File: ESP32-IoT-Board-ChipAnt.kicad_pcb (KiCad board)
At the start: 2 copper layers, 49 parts, among them IC1 ESP32-C3FH4, IC2 CP2102N-A02-GQFN28, J1 USB_B_Micro, Q1 Q_NPN_BEC, Q2 Q_NPN_BEC, U1 AMS1117-3.3, U2 USBLC6-2SC6, U3 MCP9700AT-ETT, Y1 40 Mhz Crystal

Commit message: First draft of PCB
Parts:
- removed C18: 10uF, Capacitor_SMD:C_0603_1608Metric
- removed the C3 at (160.9, 81.5)
- removed H4: MountingHole 3mm, MountingHole:MountingHole_3mm_Pad_Via
- removed MK1: INMP441ACEZ, INMP441:INMP441ACEZ
- removed R10: 10k, Resistor_SMD:R_0402_1005Metric
- removed the R3 at (144.8, 101.6)
- added C17: 10uF, Capacitor_SMD:C_0603_1608Metric, F.Cu at (150.4, 101.4)
- added J2: Conn_01x05, Connector_Molex:Molex_KK-254_AE-6410-05A_1x05_P2.54mm_Vertical, F.Cu at (138.4, 122.5)
- added R9: 10k, Resistor_SMD:R_0402_1005Metric, F.Cu at (150.1, 99.9)
- C12: renamed from C13; footprint Capacitor_SMD:C_0603_1608Metric -> Capacitor_SMD:C_0402_1005Metric
- C13: renamed from C14; footprint Capacitor_SMD:C_0603_1608Metric -> Capacitor_SMD:C_0402_1005Metric
- L2: footprint Inductor_SMD:L_0603_1608Metric -> Inductor_SMD:L_0402_1005Metric
- moved H1 73.2 mm to (123.0, 122.6)
- moved H2 56.8 mm to (123.0, 84.0)
- moved ANT1 46.7 mm to (162.8, 117.4), turned to 90 degrees
- moved Y1 41.4 mm to (145.9, 123.7), turned to 90 degrees
- moved C8 41.2 mm to (143.0, 123.8), turned to -90 degrees
- moved C13 36.4 mm to (152.1, 119.3), turned to -90 degrees
- moved C6 35.8 mm to (151.2, 124.6)
- moved C14 33.5 mm to (140.3, 115.3), turned to 180 degrees
- moved IC1 33.3 mm to (145.8, 117.1), turned to 180 degrees
- moved R6 31.6 mm to (151.8, 109.6)
- moved C5 30.2 mm to (151.2, 123.0)
- moved R1 27.3 mm to (128.6, 99.8)
- moved R4 26.8 mm to (140.3, 93.0)
- moved S1 26.2 mm to (146.0, 103.7), turned to 90 degrees
- moved L1 25.0 mm to (152.4, 115.6), turned to 180 degrees
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- renumbered C11 to C10, C12 to C11, C15 to C14, C16 to C15, C17 to C16, C4 to C3, C5 to C4, C6 to C5, C7 to C6, C8 to C7, C9 to C8, C10 to C9, R4 to R3, R5 to R4, R6 to R5, R7 to R6, R8 to R7, R9 to R8
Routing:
- net GND: track 0.00 -> 65.2 mm, vias 0 -> 59
- net +3V3: track 0.00 -> 63.7 mm, vias 0 -> 29
- net RXD0: track 0.00 -> 36.9 mm
- net TXD0: track 0.00 -> 36.5 mm
- net CHIP_EN: track 0.00 -> 30.0 mm, vias 0 -> 2
- net GPIO9: track 0.00 -> 26.9 mm, vias 0 -> 2
- net ADC_IN: track 0.00 -> 25.1 mm
- net VBUS: track 0.00 -> 19.3 mm, vias 0 -> 2
- net RTS: track 0.00 -> 14.4 mm, vias 0 -> 2
- net DTR: track 0.00 -> 14.2 mm, vias 0 -> 2
- net I2S_WS: track 0.00 -> 12.8 mm, vias 0 -> 2
- net unconnected-(J1-Pad6): track 0.00 -> 12.6 mm
- net D-: track 0.00 -> 11.9 mm
- net D+: track 0.00 -> 10.4 mm
- net I2S_SCK: track 0.00 -> 9.17 mm, vias 0 -> 2
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- added copper zone on B.Cu, net (none)
- added copper zone on F.Cu, net (none)
- added copper zone on In2.Cu, net +3V3
- added copper zone on In1.Cu, net GND
- added copper zone on F.Cu, net Net-(ANT1-Pad1)
- added copper zone on F.Cu, net unconnected-(ANT1-Pad2)
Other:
- board outline added: 45.6 x 45.6 mm
- copper layers 2 -> 4

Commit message: --
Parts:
- removed the C15 at (138.1, 108.8)
- removed IC2: CP2102N-A02-GQFN28, CP2102N-A02-GQFN28:QFN50P500X500X80-29N-D
- removed Q1, Q2: Q_NPN_BEC, Package_TO_SOT_SMD:SOT-23
- removed the R3 at (142.1, 96.4)
- removed the R4 at (140.3, 93.0)
- removed R7: 10k(NC), Resistor_SMD:R_0402_1005Metric
- removed R8: 1k, Resistor_SMD:R_0402_1005Metric
- added J3: Conn_01x05, Connector_PinHeader_2.54mm:PinHeader_1x05_P2.54mm_Vertical, F.Cu at (148.5, 96.0)
- added R5: 1k, Resistor_SMD:R_0402_1005Metric, F.Cu at (142.9, 111.4)
- J2: footprint Connector_Molex:Molex_KK-254_AE-6410-05A_1x05_P2.54mm_Vertical -> Connector_PinHeader_2.54mm:PinHeader_1x05_P2.54mm_Vertical
- moved J2 3.46 mm to (134.9, 123.0)
- moved C14 0.58 mm to (140.9, 115.3)
- moved C8 0.52 mm to (143.0, 124.3)
- renumbered C16 to C15, C17 to C16, R5 to R3, R6 to R4, R9 to R6
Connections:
- C4 pad 1: Net-(C4-Pad1) -> +3V3
- IC1 pad 25: unconnected-(IC1-Pad25) -> USBLC_D-
- IC1 pad 26: unconnected-(IC1-Pad26) -> USBLC_D+
- U3 pad 1: Net-(C4-Pad1) -> +3V3
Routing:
- net GPIO9: track 26.9 -> 3.38 mm, vias 2 -> 0
- net USBLC_D+: track 8.75 -> 30.2 mm, vias 0 -> 2
- net VBUS: track 19.3 -> 39.3 mm
- net USBLC_D-: track 6.04 -> 24.6 mm
- net RTS: track 14.4 -> 0.00 mm, vias 2 -> 0
- net DTR: track 14.2 -> 0.00 mm, vias 2 -> 0
- net RXD0: track 36.9 -> 50.5 mm, vias 0 -> 2
- net TXD0: track 36.5 -> 49.4 mm, vias 0 -> 2
- net CHIP_EN: track 30.0 -> 20.8 mm
- net GND: track 65.2 -> 59.5 mm, vias 59 -> 75
- net +3V3: track 63.7 -> 59.5 mm, vias 29 -> 27
- net I2S_WS: track 12.8 -> 8.83 mm
- net I2S_SD: track 6.42 -> 10.1 mm
- net Net-(C4-Pad1): track 1.82 -> 0.00 mm
- net Net-(Q2-Pad1): track 1.68 -> 0.00 mm
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
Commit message: Changed almost everything
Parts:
- removed FB1: 600 @ 100Mhz, Inductor_SMD:L_1206_3216Metric
- removed H1, H2, H3: MountingHole 3mm, MountingHole:MountingHole_3mm_Pad_Via
- removed the J2 at (134.9, 123.0)
- removed J3: Conn_01x05, Connector_PinHeader_2.54mm:PinHeader_1x05_P2.54mm_Vertical
- removed S1: RKB2SJM250SMTR_LFS (Button), RKB2SJM250SMTR LFS:RKB2SJM250SMTRLFS
- removed the U1 at (133.4, 89.2)
- added C3: 4.7uF, Capacitor_SMD:C_0402_1005Metric, F.Cu at (149.4, 103.7)
- added C4: 4.7uF, Capacitor_SMD:C_0402_1005Metric, F.Cu at (144.8, 100.8)
- added C5: 0.1uF, Capacitor_SMD:C_0402_1005Metric, B.Cu at (146.6, 100.3)
- added IC1: MIC5528-3.3YMT-T5, Package_DFN_QFN:TDFN-6-1EP_2.5x2.5mm_P0.65mm_EP1.3x2mm, F.Cu at (151.4, 101.8)
- added J1: LiPo Battery, Connector_JST:JST_PH_S2B-PH-K_1x02_P2.00mm_Horizontal, B.Cu at (149.8, 108.8)
- added JP1: GPIO9, Resistor_SMD:R_0402_1005Metric, F.Cu at (136.3, 104.1)
- added MK1: INMP441ACEZ, INMP441:INMP441ACEZ, B.Cu at (142.9, 102.0)
- added Q1: FDN340P, Package_TO_SOT_SMD:SOT-23, F.Cu at (147.9, 100.8)
- added R1: 10k, Resistor_SMD:R_0402_1005Metric, F.Cu at (150.3, 98.6)
- added R3: 10k, Resistor_SMD:R_0402_1005Metric, F.Cu at (141.8, 103.1)
- added R5: 100k, Resistor_SMD:R_0402_1005Metric, B.Cu at (138.8, 100.7)
- added U2: MCP73831-2-OT, Package_TO_SOT_SMD:SOT-23-5, F.Cu at (146.8, 104.3)
- C1, C2: value 10uF -> 2.2uF; footprint Capacitor_SMD:C_0603_1608Metric -> Capacitor_SMD:C_0402_1005Metric
- C10: renamed from C11; footprint Capacitor_SMD:C_0603_1608Metric -> Capacitor_SMD:C_0402_1005Metric
- C13: renamed from C7; footprint Capacitor_SMD:C_0603_1608Metric -> Capacitor_SMD:C_0402_1005Metric
- C14: renamed from C8; footprint Capacitor_SMD:C_0603_1608Metric -> Capacitor_SMD:C_0402_1005Metric
- C15: renamed from C3; footprint Capacitor_SMD:C_0603_1608Metric -> Capacitor_SMD:C_0402_1005Metric
- C16: renamed from C4; footprint Capacitor_SMD:C_0603_1608Metric -> Capacitor_SMD:C_0402_1005Metric
- C17: renamed from C14; footprint Capacitor_SMD:C_0603_1608Metric -> Capacitor_SMD:C_0402_1005Metric
- C18: renamed from C16; footprint Capacitor_SMD:C_0603_1608Metric -> Capacitor_SMD:C_0402_1005Metric
- C19: renamed from C15; footprint Capacitor_SMD:C_0603_1608Metric -> Capacitor_SMD:C_0402_1005Metric
- C6: renamed from C5; footprint Capacitor_SMD:C_0603_1608Metric -> Capacitor_SMD:C_0402_1005Metric
- C7: renamed from C6; footprint Capacitor_SMD:C_0603_1608Metric -> Capacitor_SMD:C_0402_1005Metric
- C8: renamed from C9; footprint Capacitor_SMD:C_0603_1608Metric -> Capacitor_SMD:C_0402_1005Metric
- C9: renamed from C10; footprint Capacitor_SMD:C_0603_1608Metric -> Capacitor_SMD:C_0402_1005Metric
- D1: value D_Schottky -> NSR0530HT1G; footprint Diode_SMD:D_SOD-123 -> Diode_SMD:D_SOD-323
- R2: renamed from R1; value 0R -> 100k; footprint Resistor_SMD:R_0603_1608Metric -> Resistor_SMD:R_0402_1005Metric
- R4: renamed from R2; value 1k -> 2k
- moved C2 29.9 mm to (153.5, 103.0)
- moved J2 24.6 mm to (144.0, 94.4), turned to 180 degrees
- moved C1 20.0 mm to (144.8, 101.8), turned to 180 degrees
- moved D1 18.2 mm to (147.7, 98.1)
- moved R4 17.9 mm to (146.7, 106.5)
- moved D2 16.5 mm to (143.8, 104.5), turned to 90 degrees
- moved R2 16.2 mm to (144.8, 99.8), turned to 180 degrees
- moved C16 14.6 mm to (154.5, 106.4), turned to 90 degrees
- moved C7 14.1 mm to (142.7, 113.5), turned to -90 degrees
- moved C15 13.2 mm to (149.4, 106.4), turned to 90 degrees
- moved ANT1 13.1 mm to (150.2, 114.1), turned to -138 degrees
- moved U3 12.9 mm to (152.0, 105.8)
- moved C11 11.8 mm to (146.9, 111.4)
- moved L2 11.6 mm to (145.4, 110.9)
- moved C6 11.5 mm to (142.7, 115.3), turned to -90 degrees
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- renumbered C12 to C11, C13 to C12, IC1 to IC2, J1 to J2, R4 to R6, R6 to R7, R5 to R8, R3 to R9, U2 to U1
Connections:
- net CHIP_EN renamed Net-(C18-Pad1)
- net D+ renamed /USB & Power/D-
- net D- renamed /USB & Power/D+
- net GPIO2 renamed Net-(IC2-Pad6)
- net GPIO8 renamed Net-(IC2-Pad14)
- net GPIO9 renamed Net-(IC2-Pad15)
- net XTAL_IN renamed Net-(C13-Pad1)
- net XTAL_OUT renamed Net-(C14-Pad1)
- D1 pad 1: VBUS -> Net-(C1-Pad1)
- D1 pad 2: Net-(D1-Pad2) -> VBUS
- D2 pad 2: +3V3 -> VBUS
- IC2 pad 27: TXD0 -> unconnected-(IC2-Pad27)
- IC2 pad 28: RXD0 -> unconnected-(IC2-Pad28)
- J2 pad 1: Net-(J1-Pad1) -> VBUS
- R2 pad 1: Net-(D1-Pad2) -> VBUS
- R2 pad 2: Net-(J1-Pad1) -> GND
- R4 pad 2: GND -> Net-(R4-Pad2)
- R8 pad 2: GND -> Net-(JP1-Pad1)
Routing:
- net RXD0: track 50.5 -> 0.00 mm, vias 2 -> 0
- net TXD0: track 49.4 -> 0.00 mm, vias 2 -> 0
- net +3V3: track 59.5 -> 36.1 mm, vias 27 -> 12
- net +BATT: track 0.00 -> 22.3 mm, vias 0 -> 2
- net Net-(C18-Pad1): track 20.8 -> 5.61 mm, vias 2 -> 0
- net VBUS: track 39.3 -> 25.1 mm, vias 2 -> 0
- net ADC_IN: track 25.1 -> 11.1 mm, vias 0 -> 2
- net USBLC_D+: track 30.2 -> 18.6 mm, vias 2 -> 0
- net I2S_SD: track 10.1 -> 21.3 mm, vias 2 -> 1
- net USBLC_D-: track 24.6 -> 16.2 mm
- net Net-(J1-Pad1): track 8.04 -> 0.00 mm
- net Net-(IC2-Pad6): track 8.75 -> 2.25 mm
- net /USB & Power/D+: track 11.9 -> 7.05 mm
- net Net-(R3-Pad2): track 0.00 -> 4.71 mm
- net I2S_WS: track 8.83 -> 12.6 mm, vias 2 -> 1
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- added copper zone on In1.Cu, net +3V3
- added copper zone on In2.Cu, net GND
- removed copper zone on In2.Cu, net +3V3
- removed copper zone on In1.Cu, net GND
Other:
- board size 45.6 x 45.6 mm -> 22.8 x 26.7 mm

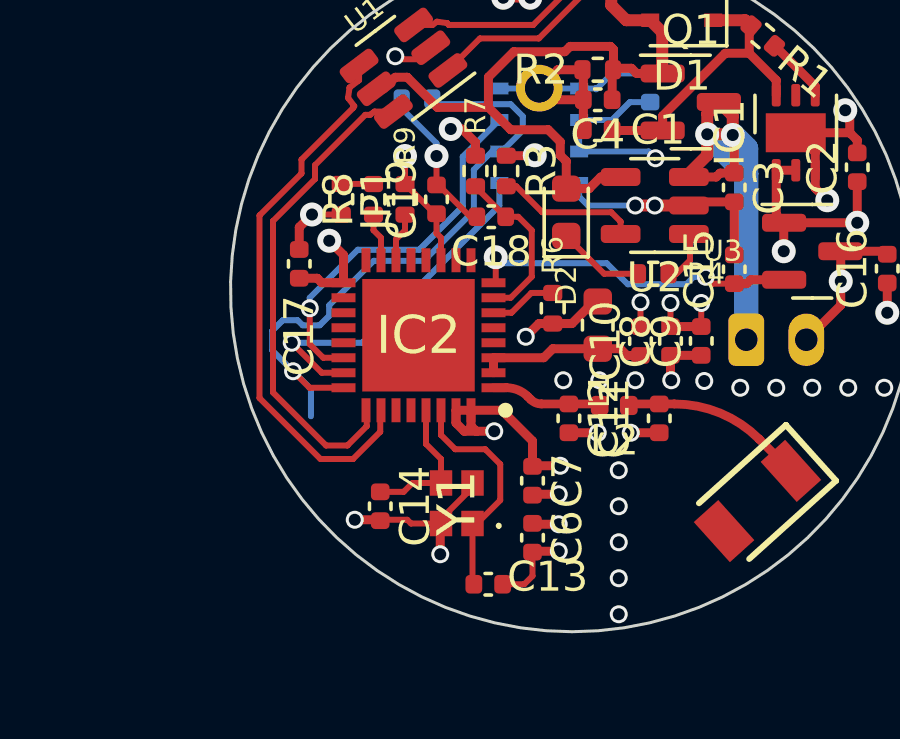
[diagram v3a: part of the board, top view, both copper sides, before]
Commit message: Added accelerometer
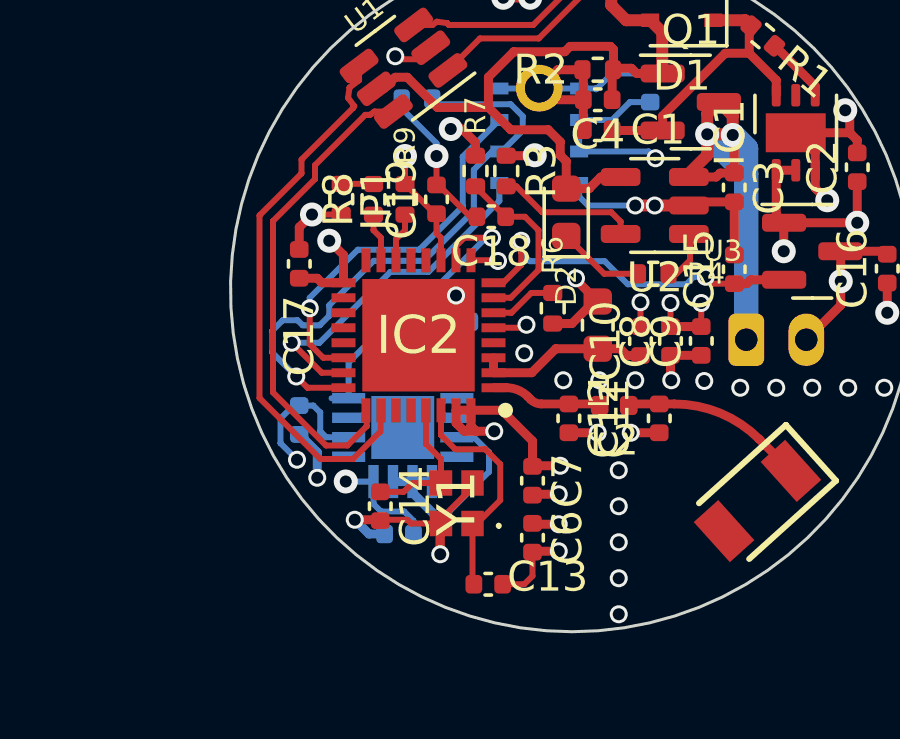
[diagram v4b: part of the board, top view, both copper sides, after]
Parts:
- added C20: 0.1uF, Capacitor_SMD:C_0402_1005Metric, B.Cu at (140.1, 108.2)
- added C21: 0.1uF, Capacitor_SMD:C_0402_1005Metric, B.Cu at (137.9, 108.1)
- added C22: 0.1uF, Capacitor_SMD:C_0402_1005Metric, B.Cu at (134.9, 111.4)
- added C23: 0.1uF, Capacitor_SMD:C_0402_1005Metric, B.Cu at (138.2, 115.2)
- added IC3: ADXL335BCPZ-RL, Package_CSP:LFCSP-16-1EP_4x4mm_P0.65mm_EP2.1x2.1mm, B.Cu at (138.3, 111.7)
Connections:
- IC2 pad 10: unconnected-(IC2-Pad10) -> XOUT
- IC2 pad 5: unconnected-(IC2-Pad5) -> ZOUT
- IC2 pad 9: unconnected-(IC2-Pad9) -> YOUT
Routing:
- net XOUT: track 0.00 -> 15.9 mm, vias 0 -> 2
- net YOUT: track 0.00 -> 15.7 mm, vias 0 -> 2
- net GND: track 58.4 -> 72.9 mm, vias 34 -> 36
- net ZOUT: track 0.00 -> 14.1 mm, vias 0 -> 2
- net Net-(IC3-Pad15): track 0.00 -> 3.10 mm
- net I2S_SD: track 21.3 -> 19.6 mm
- net ADC_IN: track 11.1 -> 11.8 mm

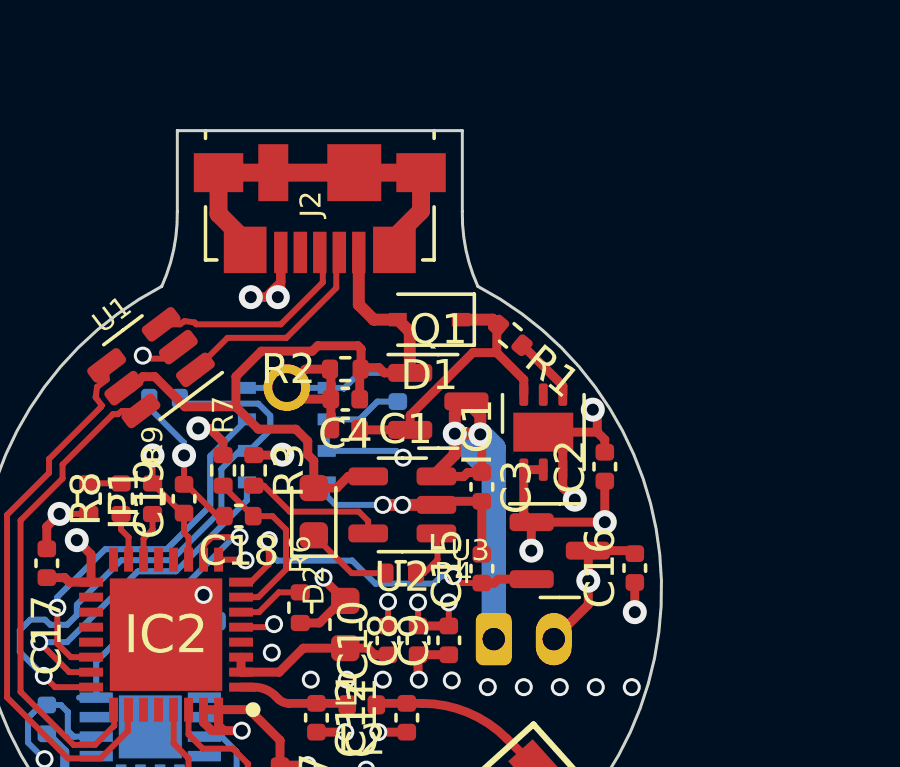
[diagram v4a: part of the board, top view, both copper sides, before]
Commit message: Made new layout
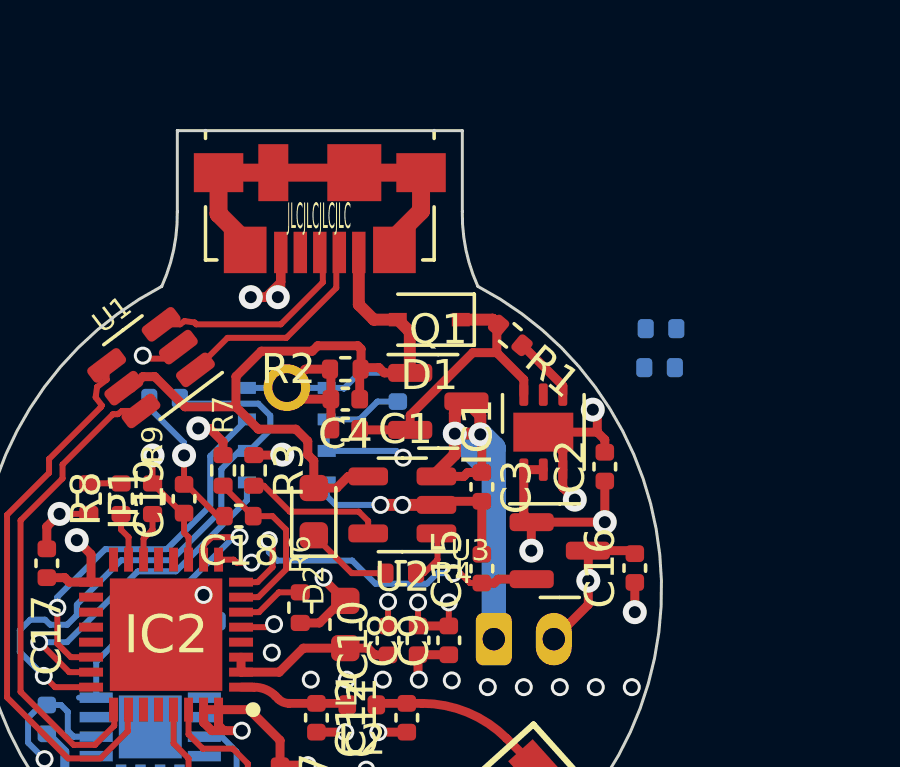
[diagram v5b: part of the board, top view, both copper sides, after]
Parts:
- added R10: 1M, Resistor_SMD:R_0402_1005Metric, B.Cu at (155.3, 99.7)
- added R11: 1M, Resistor_SMD:R_0402_1005Metric, B.Cu at (155.4, 98.4)
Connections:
- net ADC_IN renamed TEMP_OUT
- IC2 pad 4: unconnected-(IC2-Pad4) -> BAT_LVL
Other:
- board text added: "JLCJLCJLCJLC"
